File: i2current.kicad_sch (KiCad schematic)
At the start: 109 parts, among them CN1 JL15EDGA-38106G01, J1 B4P, J10 QWIIC, J11 QWIIC, J2 USB_C_Receptacle_USB2.0, J3 CONN_BATT, J4 Conn_01x12_MountingPin, J5 EXT_IFACE, J6 Conn_01x05, J8 PANEL_CONN, J9 Conn_01x06, Q1 AO3400A, Q4 AO3400A, Q5 AO3400A, Q6 AO3400A, Q8 AO3400A, SW6 SW_SPDT, U1 SPX3819M5-L-3-3, U10 SMTSO3030CTJ, U11 TPS56637RPAR, U12 A-SP1102AR6GHC-A01-2C, U13 A-SP1102AR6GHC-A01-2C, U2 SMTSO3030CTJ, U3 SMTSO3030CTJ, U4 FTC252010S4R7MBCA, U5 FUSB302B01MPX, U6 MT2492, U7 ESP32-C3-WROOM-02, U8 BQ25792RQMR, U9 SMTSO3030CTJ

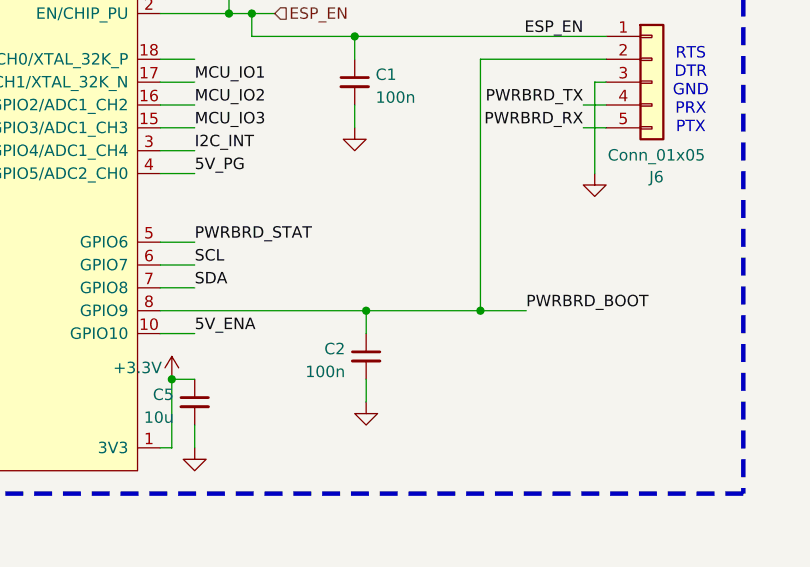
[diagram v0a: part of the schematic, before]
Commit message: add SD test
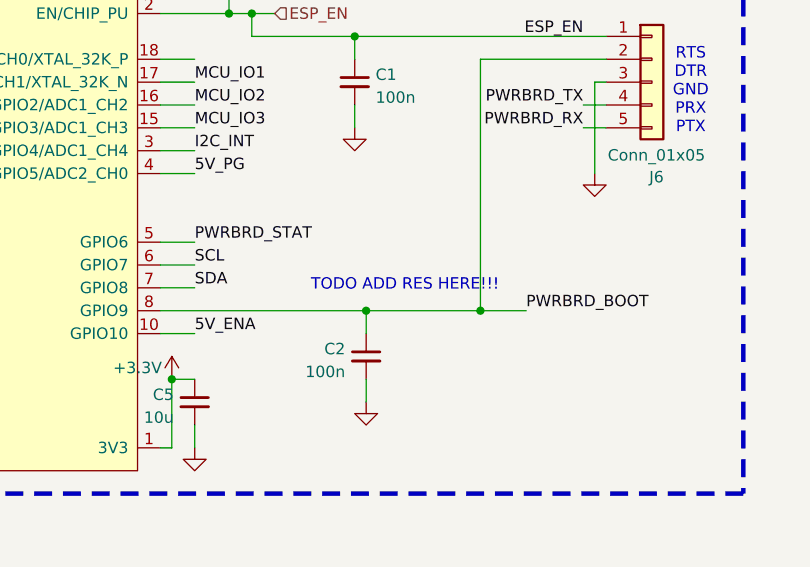
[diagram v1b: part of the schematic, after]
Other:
- note added: "TODO ADD RES HERE!!!"
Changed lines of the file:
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@@
+		)
+	)
+	(text "TODO ADD RES HERE!!!"
+		(exclude_from_sim no)
+		(at 117.348 258.826 0)
+		(effects
+			(font
+				(size 1.27 1.27)
+			)
 		)
 	)

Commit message: checkpoint for next rev
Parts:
- removed C15: 22uF/6.3V, Capacitor_SMD:C_0603_1608Metric, symbol Device:C_Small
- removed J10, J11: QWIIC, Connector_JST:JST_SH_SM04B-SRSS-TB_1x04-1MP_P1.00mm_Horizontal, symbol Connector_Generic:Conn_01x04
- removed J6: Conn_01x05, Connector_PinHeader_1.27mm:PinHeader_1x05_P1.27mm_Vertical, symbol Connector_Generic:Conn_01x05
- removed J8: PANEL_CONN, Connector_PinHeader_2.54mm:PinHeader_1x06_P2.54mm_Vertical, symbol Connector_Generic:Conn_01x06
- removed J9: Conn_01x06, Connector_JST:JST_PH_S6B-PH-K_1x06_P2.00mm_Horizontal, symbol Connector_Generic:Conn_01x06
- removed JP4: 3V3_5V, Jumper:SolderJumper-2_P1.3mm_Open_TrianglePad1.0x1.5mm, symbol Jumper:SolderJumper_2_Open
- removed Q1, Q4, Q5, Q6, Q8: AO3400A, Package_TO_SOT_SMD:SOT-23, symbol Transistor_FET:AO3400A
- removed R29: 3k, Resistor_SMD:R_0402_1005Metric, symbol Device:R_Small
- removed TP1, TP3, TP4: TestPoint, TestPoint:TestPoint_Pad_D1.0mm, symbol Connector:TestPoint
- removed U12, U13: A-SP1102AR6GHC-A01-2C, easyeda2kicad:LED-SMD_4P-L3.0-W1.5_A-SP1102AR6GHC-A01-2C, symbol easyeda2kicad:A-SP1102AR6GHC-A01-2C
- removed U7: ESP32-C3-WROOM-02, Espressif:ESP32-C3-WROOM-02, symbol Espressif:ESP32-C3-WROOM-02
- added C15: 100u/6.3/tant, Capacitor_Tantalum_SMD:CP_EIA-3528-21_Kemet-B, symbol Device:C_Polarized_Small
- added C16: 22n, Capacitor_SMD:C_0402_1005Metric, symbol Device:C_Small
- added C24, C28, C47: 10u, Capacitor_SMD:C_0603_1608Metric, symbol Device:C_Small
- added C45, C46: 100n, Capacitor_SMD:C_0402_1005Metric, symbol Device:C_Small
- added C7: 100u/6.3/tant, Capacitor_THT:CP_Radial_D8.0mm_P5.00mm, symbol Device:C_Polarized
- added D1, D3, D4: LED, LED_SMD:LED_0805_2012Metric, symbol Device:LED
- added JP2: VBUS_VPWR, Jumper:SolderJumper-2_P1.3mm_Open_TrianglePad1.0x1.5mm, symbol Jumper:SolderJumper_2_Open
- added JP5: VSYS_VBUS, Jumper:SolderJumper-2_P1.3mm_Open_TrianglePad1.0x1.5mm, symbol Jumper:SolderJumper_2_Open
- added Q1, Q2, Q3, Q6: AON7544, easyeda2kicad:DFN-8_L3.3-W3.3-P0.65-BL-2, symbol easyeda2kicad:AON7544
- added R13: 16k, Resistor_SMD:R_0603_1608Metric, symbol Device:R_Small
- added R15, R17: 100, Resistor_SMD:R_0402_1005Metric, symbol Device:R_Small
- added R22: 3k, Resistor_SMD:R_0402_1005Metric, symbol Device:R_Small
- added R26: 10k, Resistor_SMD:R_0402_1005Metric, symbol Device:R_Small
- added U12: PY32F002AW15U6TR, Package_DFN_QFN:TQFN-16-1EP_3x3mm_P0.5mm_EP1.6x1.6mm, symbol Critbit_lib:PY32F002A_QFN16
- added U7: JLC_OLED, Critbit_lib:OLED-042-JLC, symbol Critbit_lib:JLC_OLED
- C1, C2: value 100n -> 22uF/25V; footprint Capacitor_SMD:C_0402_1005Metric -> Capacitor_SMD:C_1206_3216Metric
- C26, C42, C6: value 10u -> 100n; footprint Capacitor_SMD:C_0603_1608Metric -> Capacitor_SMD:C_0402_1005Metric
- C4: value 22uF/6.3V -> 200p; footprint Capacitor_SMD:C_0603_1608Metric -> Capacitor_SMD:C_0402_1005Metric
- C41: value 22uF/6.3V -> 22uF/25V; footprint Capacitor_SMD:C_0603_1608Metric -> Capacitor_SMD:C_1206_3216Metric
- C43: value 2u2 -> 100n; footprint Capacitor_SMD:C_0603_1608Metric -> Capacitor_SMD:C_0402_1005Metric
- R1, R20, R21, R3, R33, R35, R7, R8: footprint Resistor_SMD:R_0402_1005Metric -> Resistor_SMD:R_0603_1608Metric
- R10: value 10k -> 2
- R18, R25: value 3k -> 10k
- R27, R28: value 300/0603 -> 3k; footprint Resistor_SMD:R_0603_1608Metric_Pad0.98x0.95mm_HandSolder -> Resistor_SMD:R_0402_1005Metric
- R9: value 10k -> 16k; footprint Resistor_SMD:R_0402_1005Metric -> Resistor_SMD:R_0603_1608Metric
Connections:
- net +3.3V: now also U7.8 (BS1/I2C/~{SPI}~); no longer C5.1, C8.1, C9.1, J5.20 (Pin_20), R10.2, R33.2, U4.2
- net +VDC: now also C29.2, Q2.5 (D); no longer R23.2
- net 3V3_ENA: now also U12.1 (PB1)
- net 5V_ENA: now also U12.2 (PA12)
- net BAT: now also CN1.1, J3.1 (Pin_1), R4.2, C7.1
- net GLOB_~{OFF}: now also D4.2 (A), R22.2
- net GND: now also C26.1, C42.1, C6.1, R10.1, R23.2, R24.2, R27.1, C15.2, C16.1, C24.2, C28.2, C46.1, C47.2, C7.2, D1.1 (K), U12.17 (VSS), U7.11 (DC/SDIN/SA0), U7.6 (VSS), U7.9 (CS); no longer C26.2, C29.2, C30.2, C4.2, C42.2, C43.2, C6.2, U8.13 (~{CE})
- net I2C_INT: now also U12.7 (PA1)
- net PWRBRD_BOOT: now also U12.14 (PB0); no longer C2.1
- net PWRBRD_RX: now also U12.16 (PA8)
- net PWRBRD_TX: now also U12.13 (PA7)
- net SCL: now also U12.9 (PA3), U7.12 (D0/SCLK/SCL)
- net SDA: now also U12.8 (PA2), U7.13 (D1/SDIN/SDA), U7.14 (D2/SDA)
- net VBUS: now also C30.2, JP2.1 (A), JP5.2 (B), Q1.5 (D); no longer R24.2
- net VBUS_PIN: now also Q3.5 (D), Q6.5 (D)
- net at D6.1 (K): now also Q1.4 (G), Q6.4 (G), R17.1; no longer R27.2
- net at D6.2 (A): now also Q1.1 (S), Q1.2 (S), Q1.3 (S), Q6.1 (S), Q6.2 (S), Q6.3 (S)
- net at R9.1: now also D1.2 (A)
- net at R1.1, R3.2, U11.2 (FB): now also C4.2
- net at D7.1 (K): now also Q2.4 (G), Q3.4 (G), R15.1; no longer R28.2
- net at D7.2 (A): now also Q2.1 (S), Q2.2 (S), Q2.3 (S), Q3.1 (S), Q3.2 (S), Q3.3 (S)
- net at U8.24 (SDRV): now also C16.2
- net at U8.10 (ACDRV2): now also R17.2; no longer R27.1
- net at R25.2: now also D4.1 (K)
- net at U8.11 (ACDRV1): now also R15.2; no longer R28.1
- net at R18.2: now also D3.1 (K)
- net +5V renamed VPWR
- net VPWR: now also R28.2, C15.1, JP2.2 (B), R13.2; no longer C4.1, J4.12 (Pin_12)
- net +BATT renamed SYS
- net SYS: now also C1.1, C2.1, JP5.1 (A); no longer C26.1, C6.1
- net 3V3_L renamed VMCU_L
- removed net BAT_IN: C42.1, CN1.1, J3.1 (Pin_1), R4.2
- removed net ESP_EN: C1.1, R10.1
- net MCU_IO1 renamed PY32_SWC
- net PY32_SWC: now also U12.4 (PA14-SWC)
- net MCU_IO2 renamed PY32_nRST
- net PY32_nRST: now also R26.1, U12.5 (PF2-NRST)
- net MCU_IO3 renamed PY32_SWD
- net PY32_SWD: now also U12.3 (PA13-SWD)
- net VDD renamed 3V3_SYS
- net 3V3_SYS: now also C6.2, C46.2, C47.1, D3.2 (A), R26.2, U12.15 (VCC), U7.7 (VDD); no longer C43.1
- new net: C28.1, U7.15 (VCOMH)
- new net: C24.1, C42.2, U7.16 (VCC)
- new net: C43.1, U7.1 (C2P)
- new net: C43.2, U7.2 (C2N)
- new net: C45.2, U7.3 (C1P)
- new net: C45.1, U7.4 (C1N)
- new net: C4.1, R13.1
- new net: R22.1, U12.12 (PA6)
- new net BQ_nCE: R10.2, U12.10 (PA4), U8.13 (~{CE})
- new net OLED_RST: U12.11 (PA5), U7.10 (~{RST})
- new net PY32_ADC: R27.2, R28.1, U12.6 (PA0)
- new net VMCU: C26.2, C5.1, C8.1, C9.1, J4.12 (Pin_12), J5.20 (Pin_20), R33.2, U4.2, U7.5 (VBAT)
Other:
- note added: "1n rec."
- note added: "C25977"
- note added: "Powernets description: ---------------------- Sinks: VDC: input from DC Jack or external source (like PoE shield) Bidirectional: VBUS: power from USB - careful, must not assume 5V +VBATT: terminal for battery Sources: VSYS: output from BQ charger - battery packet voltage VPWR: step-down for external heavy load (6A) VMCU: step-down source for ESP32, can be set to 5V 3V3_SYS: low power LDO for onbo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"
- note added: "TODO add tvs"
- note removed: "Powernets description: ---------------------- Sinks: +VDC: input from DC Jack or external source (like PoE shield) Sources: +BATT: output from BQ charger - battery packet voltage +VBUS: power from USB - careful, must not assume 5V +3V3: onboard step-down source for ESP32 and stuff, can be set to 5V"
- note removed: "RTS DTR GND PRX PTX"
- note removed: "TODO ADD RES HERE!!!"
- moved on the sheet: C10, C17, C18, C19, C20, C21, C22, C23, C25, C27, C29, C3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

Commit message: finish DRC
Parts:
- removed JP1: HARDRST, Jumper:SolderJumper-2_P1.3mm_Open_TrianglePad1.0x1.5mm, symbol Jumper:SolderJumper_2_Open
- removed JP2: VBUS_VPWR, Jumper:SolderJumper-2_P1.3mm_Open_TrianglePad1.0x1.5mm, symbol Jumper:SolderJumper_2_Open
- removed JP5: VSYS_VBUS, Jumper:SolderJumper-2_P1.3mm_Open_TrianglePad1.0x1.5mm, symbol Jumper:SolderJumper_2_Open
- removed L3: FXL0420-1R0-M, easyeda2kicad:IND-SMD_L4.4-W4.2, symbol easyeda2kicad:FXL0420-1R0-M
- added D2: LED, LED_SMD:LED_0805_2012Metric, symbol Device:LED
- added L2: SPM6530T-1R0M120, easyeda2kicad:IND-SMD_L7.1-W6.5-P5.60, symbol easyeda2kicad:SPM6530T-1R0M120
- added R29, R30: 0R/1206, Resistor_SMD:R_1206_3216Metric, symbol Device:R_Small
- added R32: 10k, Resistor_SMD:R_0402_1005Metric, symbol Device:R_Small
- added TP1: TestPoint, TestPoint:TestPoint_Pad_D1.0mm, symbol Connector:TestPoint
- added U13: USBLC6-4SC6, Package_TO_SOT_SMD:SOT-23-6, symbol Power_Protection:USBLC6-4SC6
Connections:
- net +3.3V is gone; now on net 3V3_SYS: U7.8 (BS1/I2C/~{SPI}~)
- net 3V3_SYS: now also U13.5 (VBUS)
- net BQ_SW1: now also L2.1
- net BQ_SW2: now also L2.2
- net CC1: now also U13.3 (I/O2)
- net CC2: now also U13.6 (I/O4)
- net GND: now also R9.1, R32.1, U13.2 (GND); no longer D1.1 (K)
- net SYS: now also R29.2
- net USBIN_M: now also U13.1 (I/O1)
- net USBIN_P: now also U13.4 (I/O3)
- net VBUS: now also R29.1, R30.2
- net VMCU: now also D2.2 (A)
- net VPWR: now also D1.2 (A), R30.1; no longer R9.2
- net AC1_FETS: now reaches D7.2 (A), Q2.1 (S), Q2.2 (S), Q2.3 (S), Q3.1 (S), Q3.2 (S), Q3.3 (S)
- net at U8.12 (~{QON}): now also TP1.1
- net AC2_FETS: now reaches D6.2 (A), Q1.1 (S), Q1.2 (S), Q1.3 (S), Q6.1 (S), Q6.2 (S), Q6.3 (S)
- new net: D1.1 (K), R9.2
- new net: D2.1 (K), R32.2
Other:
- moved on the sheet: D1, R9

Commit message: before parts
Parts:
- removed U10, U2, U3, U9: SMTSO3030CTJ, easyeda2kicad:SMD_BD5.6-D4.1, symbol easyeda2kicad:SMTSO3030CTJ
- added C48, C49: 100n, Capacitor_SMD:C_0402_1005Metric, symbol Device:C_Small
- added D10, D8, D9: SMF24CA, easyeda2kicad:SOD-123FL_L2.7-W1.8-LS3.8-BI, symbol easyeda2kicad:SMF24CA_C19077515
- added D5: 1N5819WS, Diode_SMD:D_SOD-323, symbol Device:D_Schottky
- added H1, H2, H3, H4: M3_HOLE, MountingHole:MountingHole_3.2mm_M3_DIN965_Pad, symbol Mechanical:MountingHole_Pad
- added R34, R36: 5.1k_0603, Resistor_SMD:R_0603_1608Metric, symbol Device:R_Small
- added TP10, TP11, TP12, TP13, TP14, TP5, TP6, TP7, TP8, TP9: TestPoint, TestPoint:TestPoint_Pad_D1.0mm, symbol Connector:TestPoint
- added TP15, TP16, TP3, TP4: TestPoint, TestPoint:TestPoint_Pad_D2.0mm, symbol Connector:TestPoint
- C16, R21: now not fitted
- D6, D7: LCSC (none) -> C191023; LCSC Part C191023 -> (none)
- DC1: LCSC (none) -> C500113; LCSC Part C500113 -> (none)
- J2: LCSC (none) -> C165948
- L1: LCSC (none) -> C511015; LCSC Part C511015 -> (none)
- L2: LCSC (none) -> C87572; LCSC Part C87572 -> (none)
- Q1, Q2, Q3, Q6: LCSC (none) -> C315567; LCSC Part C315567 -> (none)
- R13, R9: value 16k -> 20k_0603
- R29, R30: value 0R/1206 -> 0R_1206; now not fitted
- R3: value 10k -> 10k_0603
- R31: value 10k/0603/DNP -> 10k_0603; now not fitted
- R32: value 10k -> 20k_0603; footprint Resistor_SMD:R_0402_1005Metric -> Resistor_SMD:R_0603_1608Metric
- R35: value 16k -> 10k_0603
- R7: value 5k -> 5.6k
- R8: value 30k -> 33k
- U1: LCSC (none) -> C9055
- U11: LCSC (none) -> C841386; LCSC Part C841386 -> (none)
- U12: LCSC (none) -> C5291740
- U4: LCSC (none) -> C5832360; LCSC Part C5832360 -> (none)
- U5: LCSC (none) -> C442699
- U6: LCSC (none) -> C89358; LCSC Part C89358 -> (none)
- U8: LCSC (none) -> C2862876; LCSC Part C2862876 -> (none)
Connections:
- net +VDC: now also C48.2, D5.2 (A), D9.2 (A)
- net BAT: now also C16.2, U8.24 (SDRV), D10.2 (A)
- net CC1: now also R34.1, TP5.1
- net CC2: now also R36.1, TP6.1
- net GND: now also C48.1, C49.1, D10.1 (K), D8.1 (K), D9.1 (K), H1.1, H2.1, H3.1, H4.1, R34.2, R36.2, TP14.1, TP16.1, TP4.1, TP7.1
- net I2C_INT: now also TP10.1
- net PY32_SWC: now also TP12.1
- net PY32_SWD: now also TP13.1
- net PY32_nRST: now also TP11.1
- net SCL: now also TP9.1
- net SDA: now also TP8.1
- net VBUS: now also C49.2, D8.2 (A)
- new net: D5.1 (K), TP15.1, TP3.1
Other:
- note added: "16k -> 3v3 10k -> 5v0"
- note added: "5k/30k originally"
- note added: "C4184"
- note added: "Charging in progress (including recharge and charging in top-off timer) LOW Charging complete HIGH HIZ mode, charge disable HIGH Battery only mode and OTG mode HIGH Charge suspend (A fault condition which disable charging) Blinking at 1 Hz"
- note removed: "1n rec."
- note removed: "C157919"
- note removed: "C352437"
- note removed: "TODO add tvs"

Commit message: really before order really
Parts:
- removed D6, D7: 1N5819WS, Diode_SMD:D_SOD-323, symbol Device:D_Schottky
- removed JP3: VBUS_DC, Jumper:SolderJumper-2_P1.3mm_Open_TrianglePad1.0x1.5mm, symbol Jumper:SolderJumper_2_Open
- added D11, D6: PSM712-LF-T7, easyeda2kicad:SOT-23-3_L3.0-W1.7-P0.95-LS2.9-BR, symbol easyeda2kicad:PSM712-LF-T7
- added D12, D13, D7: LED, LED_SMD:LED_0603_1608Metric, symbol Device:LED
- added R37: 0R_0805, Resistor_SMD:R_0805_2012Metric, symbol Device:R_Small
- added R38, R39: 75k, Resistor_SMD:R_0603_1608Metric, symbol Device:R_Small
- added R40: 10k, Resistor_SMD:R_0402_1005Metric, symbol Device:R_Small
- C1, C2, C41: LCSC (none) -> C12891
- C10, C17, C18, C22, C23, C24, C28, C31, C32, C33, C34, C37, C39, C40, C47, C5: value 10u -> 10u/25V; LCSC (none) -> C96446
- C11, C12, C19, C20, C25, C26, C27, C35, C36, C38, C42, C43, C45, C46, C48, C49, C6: LCSC (none) -> C307331
- C13, C14, C4: value 200p -> 220p; LCSC (none) -> C1530
- C15: LCSC (none) -> C16133
- C16, C3: LCSC (none) -> C1532
- C21: LCSC (none) -> C23733
- C29, C30: value 2u2 -> 1u/25V; LCSC (none) -> C15849
- C44, C8, C9: LCSC (none) -> C59461
- C7: value 100u/6.3/tant -> 100u/tht
- D1, D2, D3, D4: footprint LED_SMD:LED_0805_2012Metric -> LED_SMD:LED_0603_1608Metric; LCSC C84256 -> C72038
- D10, D8, D9: LCSC (none) -> C19077515; LCSC Part C19077515 -> (none)
- D5: now not fitted
- R10, R23, R24: footprint Resistor_SMD:R_0402_1005Metric -> Resistor_SMD:R_0603_1608Metric; LCSC (none) -> C22939
- R29, R30: value 0R_1206 -> 0R_0805; footprint Resistor_SMD:R_1206_3216Metric -> Resistor_SMD:R_0805_2012Metric
- R31: footprint Resistor_SMD:R_0603_1608Metric_Pad0.98x0.95mm_HandSolder -> Resistor_SMD:R_0603_1608Metric
- SW6: LCSC (none) -> C393937; LCSC Part C393937 -> (none)
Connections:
- net +VDC: now also R37.1, R38.2
- net 3V3_SYS: now also D13.2 (A)
- net AC1_FETS: now also D6.3 (K)
- net AC2_FETS: now also D11.3 (K)
- net GND: now also D7.1 (K), R39.1
- net PWRBRD_BOOT: now also R40.1
- net VBUS: now also D12.2 (A), R37.2
- net at Q2.4 (G), Q3.4 (G), R15.1: now also D6.1 (A1), D6.2 (A1)
- net at Q1.4 (G), Q6.4 (G), R17.1: now also D11.1 (A1), D11.2 (A1)
- new net: D12.1 (K), R39.2
- new net: D7.2 (A), R38.1
- new net: D13.1 (K), R40.2
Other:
- note removed: "care, 16V mounted"
- moved on the sheet: C48, C49, Q1, Q2, Q3, Q6

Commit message: 01/25 order
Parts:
- C7: now not fitted
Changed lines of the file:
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@@
 		(in_bom yes)
 		(on_board yes)
-		(dnp no)
+		(dnp yes)
 		(property "Reference" "C7"
 			(at 222.504 65.024 0)

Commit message: PCB next rev checkpoint
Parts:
- removed C15: 100u/6.3/tant, Capacitor_Tantalum_SMD:CP_EIA-3528-21_Kemet-B, symbol Device:C_Polarized_Small
- removed C7: 100u/tht, Capacitor_THT:CP_Radial_D8.0mm_P5.00mm, symbol Device:C_Polarized
- removed CN1: JL15EDGA-38106G01, easyeda2kicad:CONN-TH_6P-P3.81_JILN_JL15EDGA-38106G01, symbol easyeda2kicad:JL15EDGA-38106G01
- removed J1: B4P, Critbit_lib:B4P_MATRIXPWR, symbol Critbit_lib:MATRIXPWR
- removed J3: CONN_BATT, Connector_JST:JST_PH_S3B-PH-K_1x03_P2.00mm_Horizontal, symbol Connector_Generic:Conn_01x03
- removed R29, R30: 0R_0805, Resistor_SMD:R_0805_2012Metric, symbol Device:R_Small
- added C15, C50: 22uF/25V, Capacitor_SMD:C_1206_3216Metric, symbol Device:C_Small
- added C51: 10u/25V, Capacitor_SMD:C_0603_1608Metric, symbol Device:C_Small
- added C7: 100n, Capacitor_SMD:C_0402_1005Metric, symbol Device:C_Small
- added CN2: JL15EDGA-38108G01, easyeda2kicad:CONN-TH_8P-P3.81_JILN_JL15EDGA-38108G01, symbol easyeda2kicad:JL15EDGA-38108G01
- added J1: Conn_01x03, teensy:CONN-TH_MR30-M, symbol Connector_Generic:Conn_01x03
- added JP1: 1S, Jumper:SolderJumper-2_P1.3mm_Open_TrianglePad1.0x1.5mm, symbol Jumper:SolderJumper_2_Open
- added JP2: 2S, Jumper:SolderJumper-2_P1.3mm_Open_TrianglePad1.0x1.5mm, symbol Jumper:SolderJumper_2_Open
- added R41, R42, R43, R44: 3k/0603, Resistor_SMD:R_0603_1608Metric, symbol Device:R_Small
- added R45: 100, Resistor_SMD:R_0402_1005Metric, symbol Device:R_Small
- added TP17, TP18, TP19: TestPoint, Critbit_lib:Nano_testpad_0.5x1.0mm, symbol Connector:TestPoint
- added TP20: TestPoint, TestPoint:TestPoint_Pad_D1.0mm, symbol Connector:TestPoint
- added U2: 74HC4066PW,118, easyeda2kicad:TSSOP-14_L5.0-W4.4-P0.65-LS6.4-BL, symbol easyeda2kicad:74HC4066PW,118
- C16: value 22n -> 1n; now fitted
- C2: value 22uF/25V -> 10u/25V; footprint Capacitor_SMD:C_1206_3216Metric -> Capacitor_SMD:C_0603_1608Metric; LCSC C12891 -> C96446
- J5: footprint Critbit_lib:2x10_smdthrough -> Critbit_lib:SAMTEC_HLE-110-02-F-DV-BE-A
- R10: value 2 -> 3k/0603; LCSC C22939 -> (none)
- R19: value 6k/0603 -> 3k; footprint Resistor_SMD:R_0603_1608Metric_Pad0.98x0.95mm_HandSolder -> Resistor_SMD:R_0402_1005Metric
- TP1: footprint TestPoint:TestPoint_Pad_D1.0mm -> Critbit_lib:Nano_testpad_0.5x1.0mm
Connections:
- net +VDC: now also D5.1 (K), CN2.8; no longer D5.2 (A)
- net 3V3_ENA: now also U2.12 (4E), U2.13 (1E), U2.5 (2E), U2.6 (3E)
- net 3V3_SYS: now also R19.2, C7.2, U2.14 (VCC)
- net BAT: now also C16.1, CN2.4; no longer C16.2, U8.24 (SDRV)
- net GLOB_~{OFF}: now also TP18.1, TP19.1
- net GND: now also U12.10 (PA4), U8.13 (~{CE}), C15.2, C50.2, C51.2, C7.1, CN2.1, CN2.3, CN2.7, J1.3 (Pin_3), JP1.2 (B), JP2.2 (B), R43.1, R44.1, TP17.1, U2.7 (GND); no longer C16.1, R10.1, R19.1
- net I2C_INT: now also U2.4 (2Y); no longer J4.6 (Pin_6), J5.14 (Pin_14), TP10.1
- net LIPO_NTC: now also CN2.5
- net OLED_RST: now also R19.1; no longer U12.11 (PA5)
- net PWRBRD_TX: now also R45.1, U2.1 (1Y); no longer J4.3 (Pin_3), J5.15 (Pin_15)
- net SCL: now also U2.11 (4Y); no longer J4.8 (Pin_8), J5.18 (Pin_18), TP9.1
- net SDA: now also U2.8 (3Y); no longer J4.7 (Pin_7), J5.16 (Pin_16), TP8.1
- net SYS: now also C51.1, CN2.6
- net VMCU: now also TP20.1
- net VPWR: now also C15.1, C50.1, CN2.2, J1.1 (Pin_1)
- net at U8.20 (PROG): now also R10.2; no longer R19.2
- net at TP15.1, TP3.1: now also D5.2 (A); no longer D5.1 (K)
- removed net BQ_nCE: R10.2, U12.10 (PA4), U8.13 (~{CE})
- new net: R41.1, R43.2, R44.2
- new net: JP2.1 (A), R41.2, R42.1
- new net: JP1.1 (A), R10.1, R42.2
- new net: C16.2, U8.24 (SDRV)
- new net: J1.2 (Pin_2), R45.2
- new net PROT_INT: J4.6 (Pin_6), J5.14 (Pin_14), TP10.1, U2.3 (2Z)
- new net PROT_SCL: J4.8 (Pin_8), J5.18 (Pin_18), TP9.1, U2.10 (4Z)
- new net PROT_SDA: J4.7 (Pin_7), J5.16 (Pin_16), TP8.1, U2.9 (3Z)
- new net PROT_TX: J4.3 (Pin_3), J5.15 (Pin_15), U2.2 (1Z)
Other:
- note added: "C4211"
- moved on the sheet: C27, C31, C32, C37, D5, J4, R31, TP10, TP8, TP9

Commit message: may order
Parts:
- removed J1: Conn_01x03, teensy:CONN-TH_MR30-M, symbol Connector_Generic:Conn_01x03
- removed R45: 100, Resistor_SMD:R_0402_1005Metric, symbol Device:R_Small
- added R29: 3k, Resistor_SMD:R_0402_1005Metric, symbol Device:R_Small
- added SW1: B2, Button_Switch_SMD:SW_SPST_TL3342, symbol Switch:SW_Push
- added TP21, TP22: TestPoint, Critbit_lib:Nano_testpad_0.5x1.0mm, symbol Connector:TestPoint
- H1, H2, H3, H4: footprint MountingHole:MountingHole_3.2mm_M3_DIN965_Pad -> Critbit_lib:MountingHole_3.2mm_LONGE
- J4: LCSC (none) -> C276921
- U2: LCSC (none) -> C5650; LCSC Part C5650 -> (none)
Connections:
- net 3V3_SYS: now also R29.2, TP22.1; no longer D13.2 (A)
- net GLOB_~{OFF}: now also TP21.1; no longer J4.1 (Pin_1)
- net GND: now also R40.1, SW1.1; no longer U12.10 (PA4)
- net PWRBRD_BOOT: no longer R40.1
- net at U12.11 (PA5): now also R22.1
- net PY32_HB_LED: now reaches U12.12 (PA6)
- net PY32_HB_LED: now also D13.2 (A); no longer R22.1
- new net PY32_BUT: R29.1, SW1.2, U12.10 (PA4)
- no-connect marks 5 -> 6
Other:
- moved on the sheet: R22
